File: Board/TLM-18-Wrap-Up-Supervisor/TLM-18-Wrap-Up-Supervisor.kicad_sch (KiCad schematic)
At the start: 18 parts, among them J1 Conn_01x02, J2 Conn_01x05, J3 Conn_01x05, U1 LM2596T-5, U2 LS7366R, U3 ADM488ANZ, Y1 AB26T-32.000kHZ

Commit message: Added photos, finished board layout, updated readme
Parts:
- removed J2, J3: Conn_01x05, symbol Connector_Generic:Conn_01x05
- added F1: Fuse, Fuse:Fuseholder_Blade_Mini_Keystone_3568, symbol Device:Fuse
- added J2: DB9_Male, Connector_Dsub:DSUB-9_Male_Vertical_P2.77x2.84mm_MountingHoles, symbol Connector:DB9_Male
- added J3: DB9_Female, Connector_Dsub:DSUB-9_Female_Vertical_P2.77x2.84mm_MountingHoles, symbol Connector:DB9_Female
- C1, C4: footprint (none) -> Capacitor_THT:C_Radial_D12.5mm_H20.0mm_P5.00mm
- C2, C3: footprint (none) -> Capacitor_THT:C_Rect_L4.0mm_W2.5mm_P2.50mm
- D1: footprint (none) -> Diode_THT:D_DO-201AD_P15.24mm_Horizontal
- D2: footprint (none) -> LED_THT:LED_D5.0mm
- J1: footprint (none) -> Connector_PinHeader_2.54mm:PinHeader_1x02_P2.54mm_Vertical
- L1: value 53uH -> 100uH; footprint (none) -> Inductor_THT:L_Radial_D12.0mm_P5.00mm_Fastron_11P
- R1, R2, R3: footprint (none) -> Resistor_THT:R_Axial_DIN0207_L6.3mm_D2.5mm_P7.62mm_Horizontal
- U2: footprint DIP762W45P254L1917H533Q14 -> TLM-18-Footprints:DIP762W45P254L1917H533Q14
- U3: footprint DIP787W46P254L953H457Q8 -> TLM-18-Footprints:DIP787W46P254L953H457Q8
- Y1: footprint (none) -> Crystal:Crystal_DS26_D2.0mm_L6.0mm_Horizontal
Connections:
- net +5V: now also J2.7
- net +VDC: now also F1.1; no longer J1.1 (Pin_1)
- net A: now also J3.7
- net B: now also J3.6
- net ENC_A: now also J2.4
- net ENC_B: now also J2.3
- net ENC_Z: now also J2.2
- net GND: now also J2.1, J2.8
- net Y: now also J3.2
- net Z: now also J3.1
- net at C2.2, U2.2 (FCKI): now also R1.1, Y1.2; no longer R1.2, Y1.1
- net at C3.2, U2.1 (FCKO): now also R1.2, Y1.1; no longer R1.1, Y1.2
- net at R2.1: now also J3.5
- new net: F1.2, J1.1 (Pin_1)
- no-connect marks 20 -> 27
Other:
- note added: "SHIELD"
- moved on the sheet: C1, C2, C3, C4, D1, D2, J1, L1, R1, R2, R3, U1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

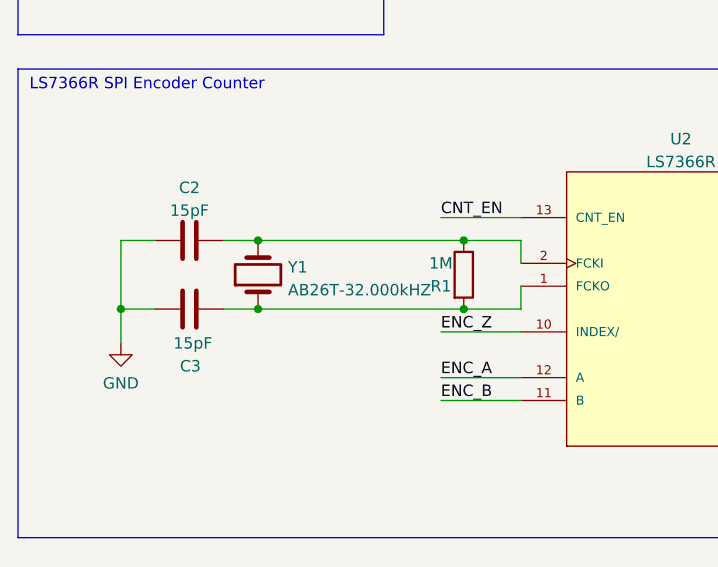
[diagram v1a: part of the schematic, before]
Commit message: Updated board SS + BOM
Changed crystal to prepackaged oscillator, added extra silkscreen marks
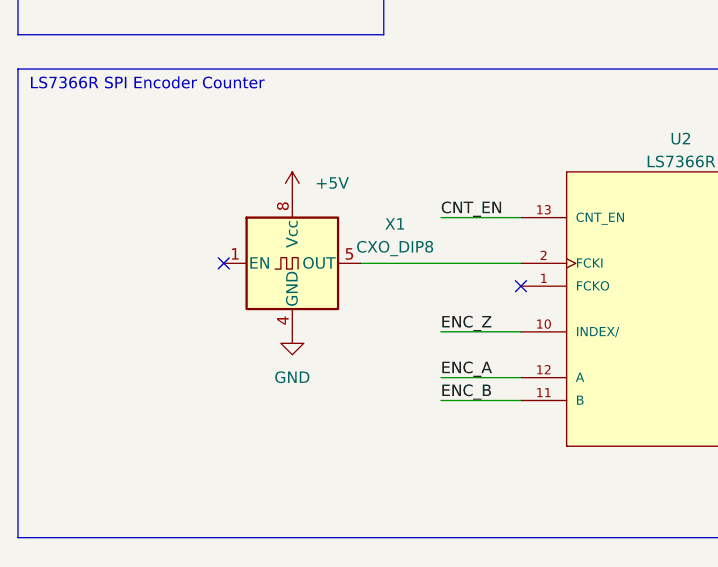
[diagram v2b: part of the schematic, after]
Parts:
- removed C2, C3: 15pF, Capacitor_THT:C_Rect_L4.0mm_W2.5mm_P2.50mm, symbol Device:C
- removed R1: 1M, Resistor_THT:R_Axial_DIN0207_L6.3mm_D2.5mm_P7.62mm_Horizontal, symbol Device:R
- removed Y1: AB26T-32.000kHZ, Crystal:Crystal_DS26_D2.0mm_L6.0mm_Horizontal, symbol Device:Crystal
- added X1: CXO_DIP8, Oscillator:Oscillator_DIP-8, symbol Oscillator:CXO_DIP8
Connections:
- net +5V: now also X1.8 (Vcc)
- net GND: now also X1.4 (GND)
- net at U2.2 (FCKI): now also X1.5 (OUT)
- no-connect marks 27 -> 29
